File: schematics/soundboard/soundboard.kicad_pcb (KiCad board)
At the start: 2 copper layers, 5 parts, among them J1 Battery, J2 Speaker, Q1 IRLZ44N, U1 DFPlayerMini, U2 STM8SF103

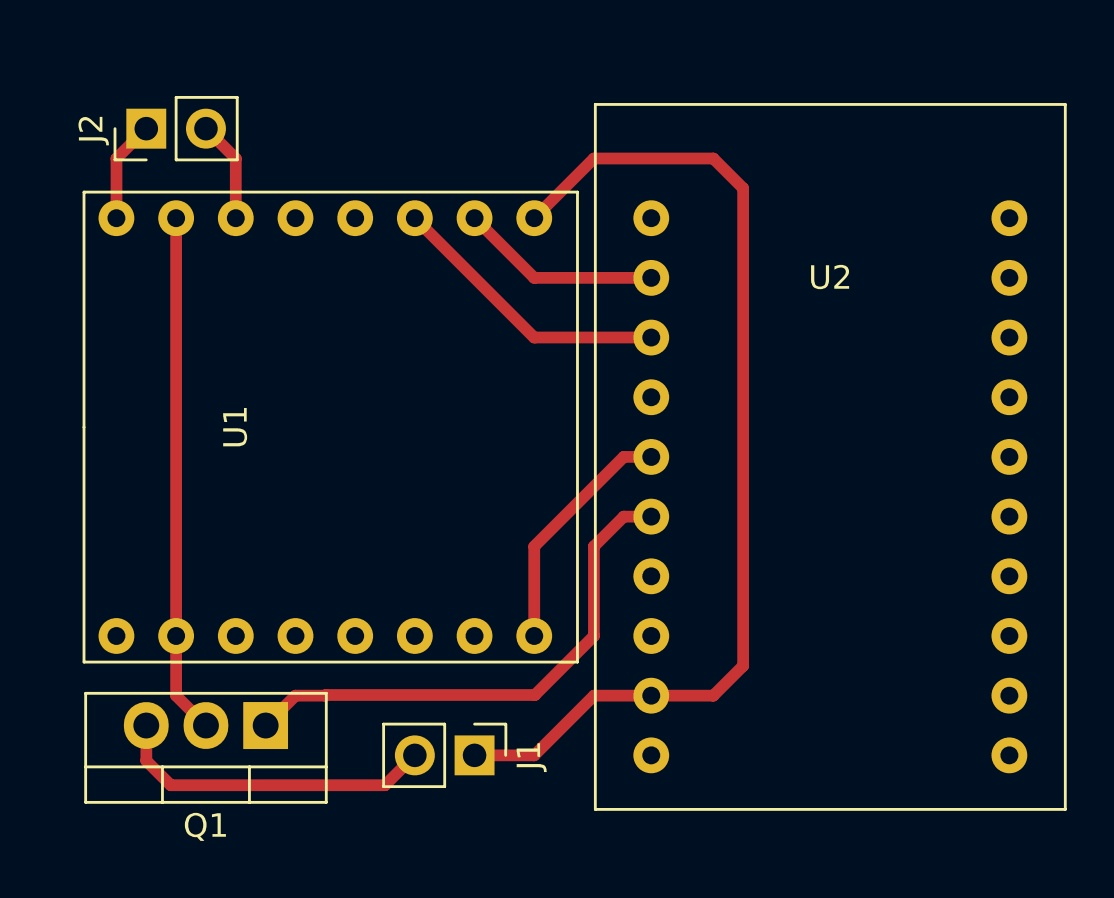
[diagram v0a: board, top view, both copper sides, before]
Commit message: Add filled zone and outlines
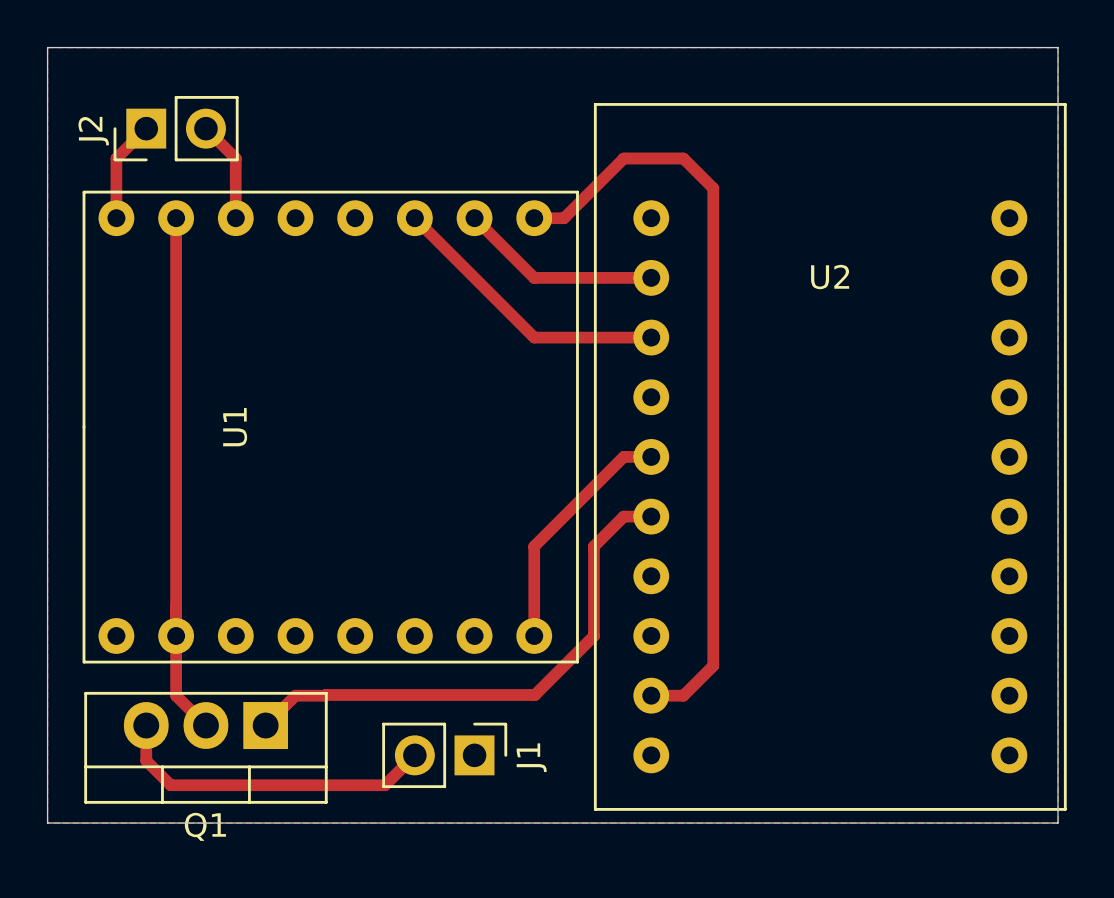
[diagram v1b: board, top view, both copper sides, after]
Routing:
- net VCC: track 43.8 -> 32.7 mm
- net Net-(Q1-Pad2): track 22.1 -> 23.4 mm
- added copper zone on F.Cu, net VCC
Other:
- board outline added: 43 x 33 mm
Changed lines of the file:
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@@
   (general
     (thickness 1.6)
-    (drawings 0)
-    (tracks 35)
+    (drawings 5)
+    (tracks 34)
     (zones 0)
     (modules 5)
@@
     (visible_elements FFFFFF7F)
     (pcbplotparams
-      (layerselection 0x010fc_ffffffff)
+      (layerselection 0x00000_7fffffff)
       (usegerberextensions false)
       (usegerberattributes false)
@@
       (padsonsilk false)
       (subtractmaskfromsilk false)
-      (outputformat 1)
-      (mirror false)
-      (drillshape 1)
+      (outputformat 4)
+      (mirror true)
+      (drillshape 0)
       (scaleselection 1)
       (outputdirectory ""))
@@
       (net 29 "Net-(U2-Pad20)"))
   )
-  (segment (start 100.33 68.58) (end 97.690001 68.58) (width 0.5) (layer F.Cu) (net 1))
-  (segment (start 101.6 67.31) (end 100.33 68.58) (width 0.5) (layer F.Cu) (net 1))
-  (segment (start 101.6 46.99) (end 101.6 67.31) (width 0.5) (layer F.Cu) (net 1))
-  (segment (start 100.33 45.72) (end 101.6 46.99) (width 0.5) (layer F.Cu) (net 1))
-  (segment (start 92.71 48.26) (end 95.25 45.72) (width 0.5) (layer F.Cu) (net 1))
-  (segment (start 95.25 45.72) (end 100.33 45.72) (width 0.5) (layer F.Cu) (net 1))
-  (segment (start 97.690001 68.58) (end 95.25 68.58) (width 0.5) (layer F.Cu) (net 1))
-  (segment (start 92.71 71.12) (end 90.17 71.12) (width 0.5) (layer F.Cu) (net 1))
-  (segment (start 95.25 68.58) (end 92.71 71.12) (width 0.5) (layer F.Cu) (net 1))
+  (gr_line (start 72 41) (end 73 41) (layer Edge.Cuts) (width 0.05))
+  (gr_line (start 72 74) (end 72 41) (layer Edge.Cuts) (width 0.05))
+  (gr_line (start 115 74) (end 72 74) (layer Edge.Cuts) (width 0.05))
+  (gr_line (start 115 41) (end 115 74) (layer Edge.Cuts) (width 0.05))
+  (gr_line (start 73 41) (end 115 41) (layer Edge.Cuts) (width 0.05))
+  (segment (start 97.690001 68.58) (end 99.06 68.58) (width 0.5) (layer F.Cu) (net 1))
+  (segment (start 92.71 48.26) (end 93.98 48.26) (width 0.5) (layer F.Cu) (net 1))
+  (segment (start 93.98 48.26) (end 96.52 45.72) (width 0.5) (layer F.Cu) (net 1))
+  (segment (start 96.52 45.72) (end 99.06 45.72) (width 0.5) (layer F.Cu) (net 1))
+  (segment (start 99.06 45.72) (end 100.33 46.99) (width 0.5) (layer F.Cu) (net 1))
+  (segment (start 100.33 46.99) (end 100.33 67.31) (width 0.5) (layer F.Cu) (net 1))
+  (segment (start 100.33 67.31) (end 99.06 68.58) (width 0.5) (layer F.Cu) (net 1))
   (segment (start 76.2 71.35) (end 77.24 72.39) (width 0.5) (layer F.Cu) (net 2))
   (segment (start 76.2 69.85) (end 76.2 71.35) (width 0.5) (layer F.Cu) (net 2))
@@
   (segment (start 83.82 68.58) (end 82.55 68.58) (width 0.5) (layer F.Cu) (net 5))
   (segment (start 82.55 68.58) (end 81.28 69.85) (width 0.5) (layer F.Cu) (net 5))
-  (segment (start 77.47 48.26) (end 77.47 66.04) (width 0.5) (layer F.Cu) (net 6))
   (segment (start 77.47 66.04) (end 77.47 68.58) (width 0.5) (layer F.Cu) (net 6))
   (segment (start 77.47 68.58) (end 78.74 69.85) (width 0.5) (layer F.Cu) (net 6))
+  (segment (start 77.47 66.04) (end 77.47 64.77) (width 0.5) (layer F.Cu) (net 6))
+  (segment (start 77.47 66.04) (end 77.47 48.26) (width 0.5) (layer F.Cu) (net 6))
   (segment (start 92.71 50.8) (end 90.17 48.26) (width 0.5) (layer F.Cu) (net 7))
   (segment (start 97.690001 50.8) (end 92.71 50.8) (width 0.5) (layer F.Cu) (net 7))
@@
   (segment (start 92.71 62.23) (end 92.71 66.04) (width 0.5) (layer F.Cu) (net 17))
   (segment (start 96.52 58.42) (end 92.71 62.23) (width 0.5) (layer F.Cu) (net 17))
+  (zone (net 1) (net_name VCC) (layer F.Cu) (hatch edge 0.508)
+    (connect_pads (clearance 0.508))
+    (min_thickness 0.254)
+    (fill yes (arc_segments 32) (thermal_gap 0.508) (thermal_bridge_width 0.508))
+    (polygon
+      (pts
+        (xy 72 41) (xy 115 41) (xy 115 74) (xy 72 74)
+      )
+    )
+  )
 )
